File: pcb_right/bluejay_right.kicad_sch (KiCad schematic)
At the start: 69 parts, among them J2 SJ-43514, U2 MCP23017

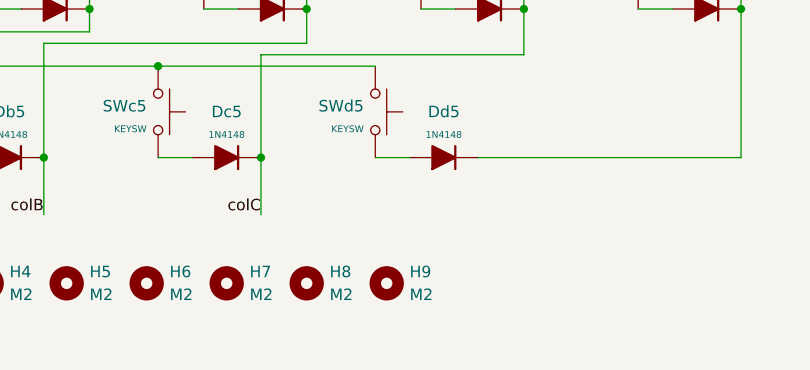
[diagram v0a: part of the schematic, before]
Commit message: remove mounting hole 9
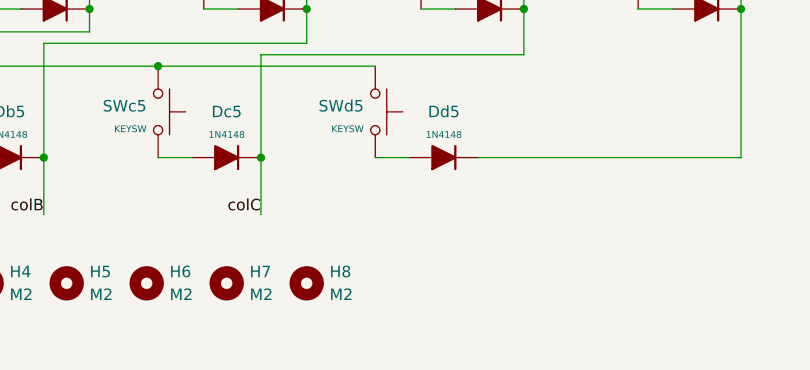
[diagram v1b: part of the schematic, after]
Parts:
- removed H9: M2, MountingHole:MountingHole_2.2mm_M2_Pad, symbol Mechanical:MountingHole
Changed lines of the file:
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@@
     (pin "1")
-  )
-  (symbol (lib_id "Mechanical:MountingHole") (at 167.64 152.4 0) (unit 1)
-    (in_bom no) (on_board yes) (fields_autoplaced)
-    (property "Reference" "H9" (id 0) (at 170.18 151.1299 0)
-      (effects (font (size 1.27 1.27)) (justify left))
-    )
-    (property "Value" "M2" (id 1) (at 170.18 153.6699 0)
-      (effects (font (size 1.27 1.27)) (justify left))
-    )
-    (property "Footprint" "MountingHole:MountingHole_2.2mm_M2_Pad" (id 2) (at 167.64 152.4 0)
-      (effects (font (size 1.27 1.27)) hide)
-    )
-    (property "Datasheet" "~" (id 3) (at 167.64 152.4 0)
-      (effects (font (size 1.27 1.27)) hide)
-    )
   )
   (symbol (lib_id "BlueJaySymbolLibrary:Switch_SW_Push") (at 195.58 91.44 270) (mirror x) (unit 1)
@@
       (reference "H8") (unit 1) (value "M2") (footprint "MountingHole:MountingHole_2.2mm_M2_Pad")
     )
-    (path "/2f72a678-d445-4b98-b401-be2796bd34c3"
-      (reference "H9") (unit 1) (value "M2") (footprint "MountingHole:MountingHole_2.2mm_M2_Pad")
-    )
     (path "/36a90cbb-ec70-4202-aacd-9cf629bac560"

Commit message: Update placement of some components and size of drill holes
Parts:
- removed H7, H8: M2, MountingHole:MountingHole_2.2mm_M2_Pad, symbol Mechanical:MountingHole
- H2: symbol Mechanical:MountingHole_Pad -> Mechanical:MountingHole
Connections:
- net GND: no longer H2.1
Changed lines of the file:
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@@
   (junction (at 171.45 86.36) (diameter 0) (color 0 0 0 0)
-  )
-  (junction (at 105.41 157.48) (diameter 0) (color 0 0 0 0)
   )
   (no_connect (at 63.5 99.06))
@@
     (stroke (width 0) (type default) (color 0 0 0 0))
   )
-  (wire (pts (xy 114.3 157.48) (xy 105.41 157.48))
-    (stroke (width 0) (type default) (color 0 0 0 0))
-  )
   (wire (pts (xy 134.62 83.82) (xy 134.62 96.52))
     (stroke (width 0) (type default) (color 0 0 0 0))
@@
   )
   (wire (pts (xy 223.52 83.82) (xy 219.71 83.82))
-    (stroke (width 0) (type default) (color 0 0 0 0))
-  )
-  (wire (pts (xy 105.41 154.94) (xy 105.41 157.48))
     (stroke (width 0) (type default) (color 0 0 0 0))
   )
@@
     (pin "1")
     (pin "2")
-  )
-  (symbol (lib_id "Mechanical:MountingHole") (at 149.86 152.4 0) (unit 1)
-    (in_bom no) (on_board yes) (fields_autoplaced)
-    (property "Reference" "H7" (id 0) (at 152.4 151.1299 0)
-      (effects (font (size 1.27 1.27)) (justify left))
-    )
-    (property "Value" "M2" (id 1) (at 152.4 153.6699 0)
-      (effects (font (size 1.27 1.27)) (justify left))
-    )
-    (property "Footprint" "MountingHole:MountingHole_2.2mm_M2_Pad" (id 2) (at 149.86 152.4 0)
-      (effects (font (size 1.27 1.27)) hide)
-    )
-    (property "Datasheet" "~" (id 3) (at 149.86 152.4 0)
-      (effects (font (size 1.27 1.27)) hide)
-    )
   )
   (symbol (lib_id "BlueJaySymbolLibrary:Interface_Expansion_MCP23017_SP") (at 45.72 109.22 0) (unit 1)
@@
     (pin "2")
   )
-  (symbol (lib_id "Mechanical:MountingHole_Pad") (at 105.41 152.4 0) (unit 1)
+  (symbol (lib_name "MountingHole_1") (lib_id "Mechanical:MountingHole") (at 105.41 152.4 0) (unit 1)
     (in_bom yes) (on_board yes) (fields_autoplaced)
     (property "Reference" "H2" (id 0) (at 107.95 151.1299 0)
@@
       (effects (font (size 1.27 1.27)) hide)
     )
-    (pin "1")
   )
   (symbol (lib_id "power:GND") (at 45.72 139.7 0) (unit 1)
@@
     (pin "2")
   )
-  (symbol (lib_id "power:GND") (at 105.41 157.48 0) (unit 1)
-    (in_bom yes) (on_board yes) (fields_autoplaced)
-    (property "Reference" "#PWR0110" (id 0) (at 105.41 163.83 0)
-      (effects (font (size 1.27 1.27)) hide)
-    )
-    (property "Value" "GND" (id 1) (at 105.41 161.29 0)
-      (effects (font (size 1.27 1.27)) hide)
-    )
-    (property "Footprint" "" (id 2) (at 105.41 157.48 0)
-      (effects (font (size 1.27 1.27)) hide)
-    )
-    (property "Datasheet" "~" (id 3) (at 105.41 157.48 0)
+  (symbol (lib_id "power:GND") (at 114.3 157.48 0) (unit 1)
+    (in_bom yes) (on_board yes) (fields_autoplaced)
+    (property "Reference" "#PWR0110" (id 0) (at 114.3 163.83 0)
+      (effects (font (size 1.27 1.27)) hide)
+    )
+    (property "Value" "GND" (id 1) (at 114.3 161.29 0)
+      (effects (font (size 1.27 1.27)) hide)
+    )
+    (property "Footprint" "" (id 2) (at 114.3 157.48 0)
+      (effects (font (size 1.27 1.27)) hide)
+    )
+    (property "Datasheet" "~" (id 3) (at 114.3 157.48 0)
       (effects (font (size 1.27 1.27)) hide)
     )
@@
     (pin "1")
   )
-  (symbol (lib_id "Mechanical:MountingHole") (at 158.75 152.4 0) (unit 1)
-    (in_bom no) (on_board yes) (fields_autoplaced)
-    (property "Reference" "H8" (id 0) (at 161.29 151.1299 0)
-      (effects (font (size 1.27 1.27)) (justify left))
-    )
-    (property "Value" "M2" (id 1) (at 161.29 153.6699 0)
-      (effects (font (size 1.27 1.27)) (justify left))
-    )
-    (property "Footprint" "MountingHole:MountingHole_2.2mm_M2_Pad" (id 2) (at 158.75 152.4 0)
-      (effects (font (size 1.27 1.27)) hide)
-    )
-    (property "Datasheet" "~" (id 3) (at 158.75 152.4 0)
-      (effects (font (size 1.27 1.27)) hide)
-    )
-  )
   (symbol (lib_id "Diode_AKL:1N4148") (at 154.94 109.22 0) (mirror x) (unit 1)
     (in_bom yes) (on_board yes) (fields_autoplaced)
@@
       (reference "H6") (unit 1) (value "M2") (footprint "MountingHole:MountingHole_2.2mm_M2_Pad")
     )
-    (path "/122e03f9-b490-4614-ab57-8a45c16d7cab"
-      (reference "H7") (unit 1) (value "M2") (footprint "MountingHole:MountingHole_2.2mm_M2_Pad")
-    )
-    (path "/ef6bf8a6-53c5-40a0-b55f-f0f6022fe6b3"
-      (reference "H8") (unit 1) (value "M2") (footprint "MountingHole:MountingHole_2.2mm_M2_Pad")
-    )
     (path "/36a90cbb-ec70-4202-aacd-9cf629bac560"
